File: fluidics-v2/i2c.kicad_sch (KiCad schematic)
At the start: 4 parts, among them U3 LTC4311CSC6-TRPBF

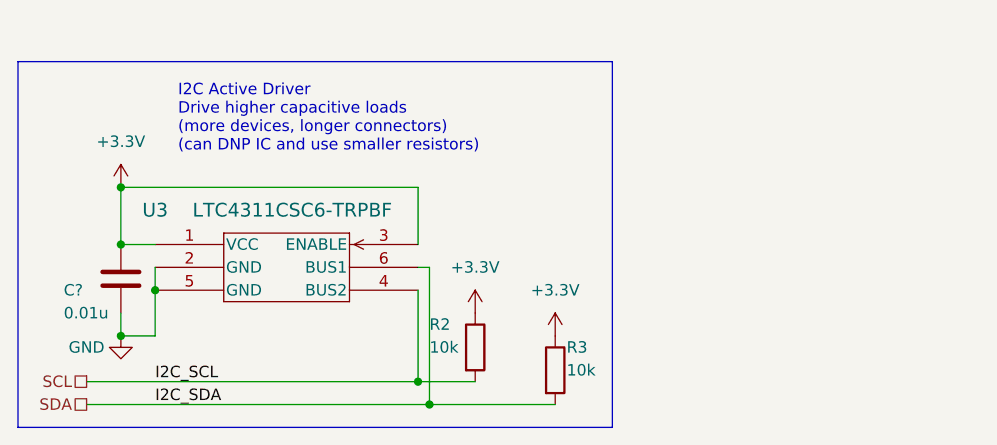
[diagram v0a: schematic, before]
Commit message: added new connector for motor control daughter board. began layout
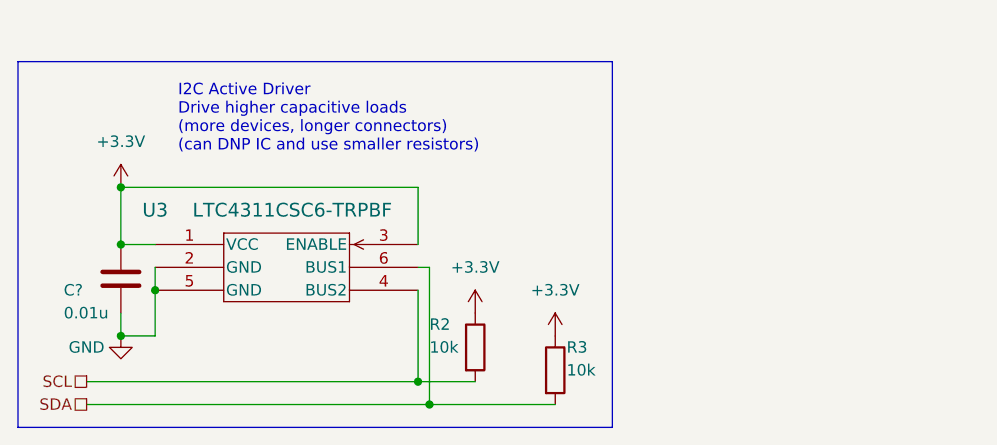
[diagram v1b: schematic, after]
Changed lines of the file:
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@@
-    (effects (font (size 1.27 1.27)) (justify left bottom))
-  )
-  (label "I2C_SDA" (at 110.49 85.09 0) (fields_autoplaced)
-    (effects (font (size 1.27 1.27)) (justify left bottom))
-  )
-  (label "I2C_SCL" (at 110.49 82.55 0) (fields_autoplaced)
     (effects (font (size 1.27 1.27)) (justify left bottom))
   )
@@
         )
         (path "/0ec91c42-8aad-437d-8c85-5e10f0e51fe0/c92aed05-d6a3-4537-8c75-2189a3bda85b"
-          (reference "U13") (unit 1)
-        )
-        (path "/0ec91c42-8aad-437d-8c85-5e10f0e51fe0/e24edef9-66ab-4bf9-965f-6f56c8fd712a"
-          (reference "U3") (unit 1)
-        )
-        (path "/0ec91c42-8aad-437d-8c85-5e10f0e51fe0/b627bb7a-5c26-4d4a-8ee1-9b58f0107eeb"
-          (reference "U14") (unit 1)
+          (reference "U10") (unit 1)
+        )
+        (path "/0ec91c42-8aad-437d-8c85-5e10f0e51fe0/e24edef9-66ab-4bf9-965f-6f56c8fd712a"
+          (reference "U8") (unit 1)
+        )
+        (path "/0ec91c42-8aad-437d-8c85-5e10f0e51fe0/b627bb7a-5c26-4d4a-8ee1-9b58f0107eeb"
+          (reference "U9") (unit 1)
         )
       )
@@
         )
         (path "/0ec91c42-8aad-437d-8c85-5e10f0e51fe0/c92aed05-d6a3-4537-8c75-2189a3bda85b"
-          (reference "R48") (unit 1)
-        )
-        (path "/0ec91c42-8aad-437d-8c85-5e10f0e51fe0/e24edef9-66ab-4bf9-965f-6f56c8fd712a"
-          (reference "R3") (unit 1)
-        )
-        (path "/0ec91c42-8aad-437d-8c85-5e10f0e51fe0/b627bb7a-5c26-4d4a-8ee1-9b58f0107eeb"
-          (reference "R50") (unit 1)
+          (reference "R44") (unit 1)
+        )
+        (path "/0ec91c42-8aad-437d-8c85-5e10f0e51fe0/e24edef9-66ab-4bf9-965f-6f56c8fd712a"
+          (reference "R40") (unit 1)
+        )
+        (path "/0ec91c42-8aad-437d-8c85-5e10f0e51fe0/b627bb7a-5c26-4d4a-8ee1-9b58f0107eeb"
+          (reference "R42") (unit 1)
         )
       )
@@
         )
         (path "/0ec91c42-8aad-437d-8c85-5e10f0e51fe0/c92aed05-d6a3-4537-8c75-2189a3bda85b"
-          (reference "R47") (unit 1)
-        )
-        (path "/0ec91c42-8aad-437d-8c85-5e10f0e51fe0/e24edef9-66ab-4bf9-965f-6f56c8fd712a"
-          (reference "R2") (unit 1)
-        )
-        (path "/0ec91c42-8aad-437d-8c85-5e10f0e51fe0/b627bb7a-5c26-4d4a-8ee1-9b58f0107eeb"
-          (reference "R49") (unit 1)
+          (reference "R43") (unit 1)
+        )
+        (path "/0ec91c42-8aad-437d-8c85-5e10f0e51fe0/e24edef9-66ab-4bf9-965f-6f56c8fd712a"
+          (reference "R39") (unit 1)
+        )
+        (path "/0ec91c42-8aad-437d-8c85-5e10f0e51fe0/b627bb7a-5c26-4d4a-8ee1-9b58f0107eeb"
+          (reference "R41") (unit 1)
         )
       )
@@
         )
         (path "/0ec91c42-8aad-437d-8c85-5e10f0e51fe0/c92aed05-d6a3-4537-8c75-2189a3bda85b"
-          (reference "#PWR0160") (unit 1)
-        )
-        (path "/0ec91c42-8aad-437d-8c85-5e10f0e51fe0/e24edef9-66ab-4bf9-965f-6f56c8fd712a"
-          (reference "#PWR034") (unit 1)
-        )
-        (path "/0ec91c42-8aad-437d-8c85-5e10f0e51fe0/b627bb7a-5c26-4d4a-8ee1-9b58f0107eeb"
-          (reference "#PWR0164") (unit 1)
+          (reference "#PWR0137") (unit 1)
+        )
+        (path "/0ec91c42-8aad-437d-8c85-5e10f0e51fe0/e24edef9-66ab-4bf9-965f-6f56c8fd712a"
+          (reference "#PWR0129") (unit 1)
+        )
+        (path "/0ec91c42-8aad-437d-8c85-5e10f0e51fe0/b627bb7a-5c26-4d4a-8ee1-9b58f0107eeb"
+          (reference "#PWR0133") (unit 1)
         )
       )
@@
         )
         (path "/0ec91c42-8aad-437d-8c85-5e10f0e51fe0/c92aed05-d6a3-4537-8c75-2189a3bda85b"
-          (reference "#PWR0159") (unit 1)
-        )
-        (path "/0ec91c42-8aad-437d-8c85-5e10f0e51fe0/e24edef9-66ab-4bf9-965f-6f56c8fd712a"
-          (reference "#PWR029") (unit 1)
-        )
-        (path "/0ec91c42-8aad-437d-8c85-5e10f0e51fe0/b627bb7a-5c26-4d4a-8ee1-9b58f0107eeb"
-          (reference "#PWR0163") (unit 1)
+          (reference "#PWR0136") (unit 1)
+        )
+        (path "/0ec91c42-8aad-437d-8c85-5e10f0e51fe0/e24edef9-66ab-4bf9-965f-6f56c8fd712a"
+          (reference "#PWR0128") (unit 1)
+        )
+        (path "/0ec91c42-8aad-437d-8c85-5e10f0e51fe0/b627bb7a-5c26-4d4a-8ee1-9b58f0107eeb"
+          (reference "#PWR0132") (unit 1)
         )
       )
@@
         )
         (path "/0ec91c42-8aad-437d-8c85-5e10f0e51fe0/c92aed05-d6a3-4537-8c75-2189a3bda85b"
-          (reference "C33") (unit 1)
-        )
-        (path "/0ec91c42-8aad-437d-8c85-5e10f0e51fe0/e24edef9-66ab-4bf9-965f-6f56c8fd712a"
-          (reference "C1") (unit 1)
-        )
-        (path "/0ec91c42-8aad-437d-8c85-5e10f0e51fe0/b627bb7a-5c26-4d4a-8ee1-9b58f0107eeb"
-          (reference "C34") (unit 1)
+          (reference "C14") (unit 1)
+        )
+        (path "/0ec91c42-8aad-437d-8c85-5e10f0e51fe0/e24edef9-66ab-4bf9-965f-6f56c8fd712a"
+          (reference "C12") (unit 1)
+        )
+        (path "/0ec91c42-8aad-437d-8c85-5e10f0e51fe0/b627bb7a-5c26-4d4a-8ee1-9b58f0107eeb"
+          (reference "C13") (unit 1)
         )
       )
@@
         )
         (path "/0ec91c42-8aad-437d-8c85-5e10f0e51fe0/c92aed05-d6a3-4537-8c75-2189a3bda85b"
-          (reference "#PWR0158") (unit 1)
-        )
-        (path "/0ec91c42-8aad-437d-8c85-5e10f0e51fe0/e24edef9-66ab-4bf9-965f-6f56c8fd712a"
-          (reference "#PWR028") (unit 1)
-        )
-        (path "/0ec91c42-8aad-437d-8c85-5e10f0e51fe0/b627bb7a-5c26-4d4a-8ee1-9b58f0107eeb"
-          (reference "#PWR0162") (unit 1)
+          (reference "#PWR0135") (unit 1)
+        )
+        (path "/0ec91c42-8aad-437d-8c85-5e10f0e51fe0/e24edef9-66ab-4bf9-965f-6f56c8fd712a"
+          (reference "#PWR0127") (unit 1)
+        )
+        (path "/0ec91c42-8aad-437d-8c85-5e10f0e51fe0/b627bb7a-5c26-4d4a-8ee1-9b58f0107eeb"
+          (reference "#PWR0131") (unit 1)
         )
       )
@@
         )
         (path "/0ec91c42-8aad-437d-8c85-5e10f0e51fe0/c92aed05-d6a3-4537-8c75-2189a3bda85b"
-          (reference "#PWR0161") (unit 1)
-        )
-        (path "/0ec91c42-8aad-437d-8c85-5e10f0e51fe0/e24edef9-66ab-4bf9-965f-6f56c8fd712a"
-          (reference "#PWR036") (unit 1)
-        )
-        (path "/0ec91c42-8aad-437d-8c85-5e10f0e51fe0/b627bb7a-5c26-4d4a-8ee1-9b58f0107eeb"
-          (reference "#PWR0165") (unit 1)
-        )
-      )
+          (reference "#PWR0138") (unit 1)
+        )
+        (path "/0ec91c42-8aad-437d-8c85-5e10f0e51fe0/e24edef9-66ab-4bf9-965f-6f56c8fd712a"
+          (reference "#PWR0130") (unit 1)
+        )
+        (path "/0ec91c42-8aad-437d-8c85-5e10f0e51fe0/b627bb7a-5c26-4d4a-8ee1-9b58f0107eeb"
+          (reference "#PWR0134") (unit 1)
+        )
+      )

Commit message: added pullups/downs to spi for stability, rounded corners
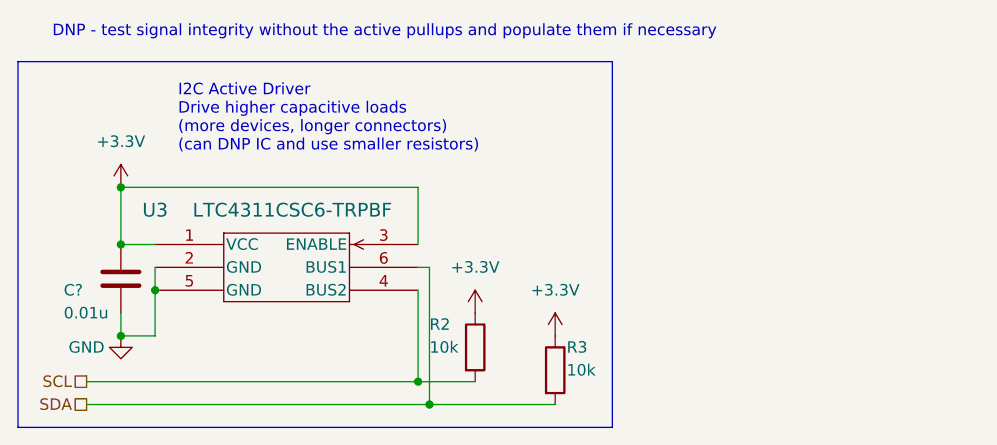
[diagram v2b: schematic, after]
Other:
- note added: "DNP - test signal integrity without the active pullups and populate them if necessary"
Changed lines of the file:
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@@
     (fill (type none))
+  )
+  (text "DNP - test signal integrity without the active pullups and populate them if necessary"
+    (at 99.06 44.45 0)
+    (effects (font (size 1.27 1.27)) (justify left bottom))
   )
   (text "I2C Active Driver\nDrive higher capacitive loads\n(more devices, longer connectors)\n(can DNP IC and use smaller resistors)"
